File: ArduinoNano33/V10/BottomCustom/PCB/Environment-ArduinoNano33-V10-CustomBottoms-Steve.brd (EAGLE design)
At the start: 71 x 34 mm, 4 parts

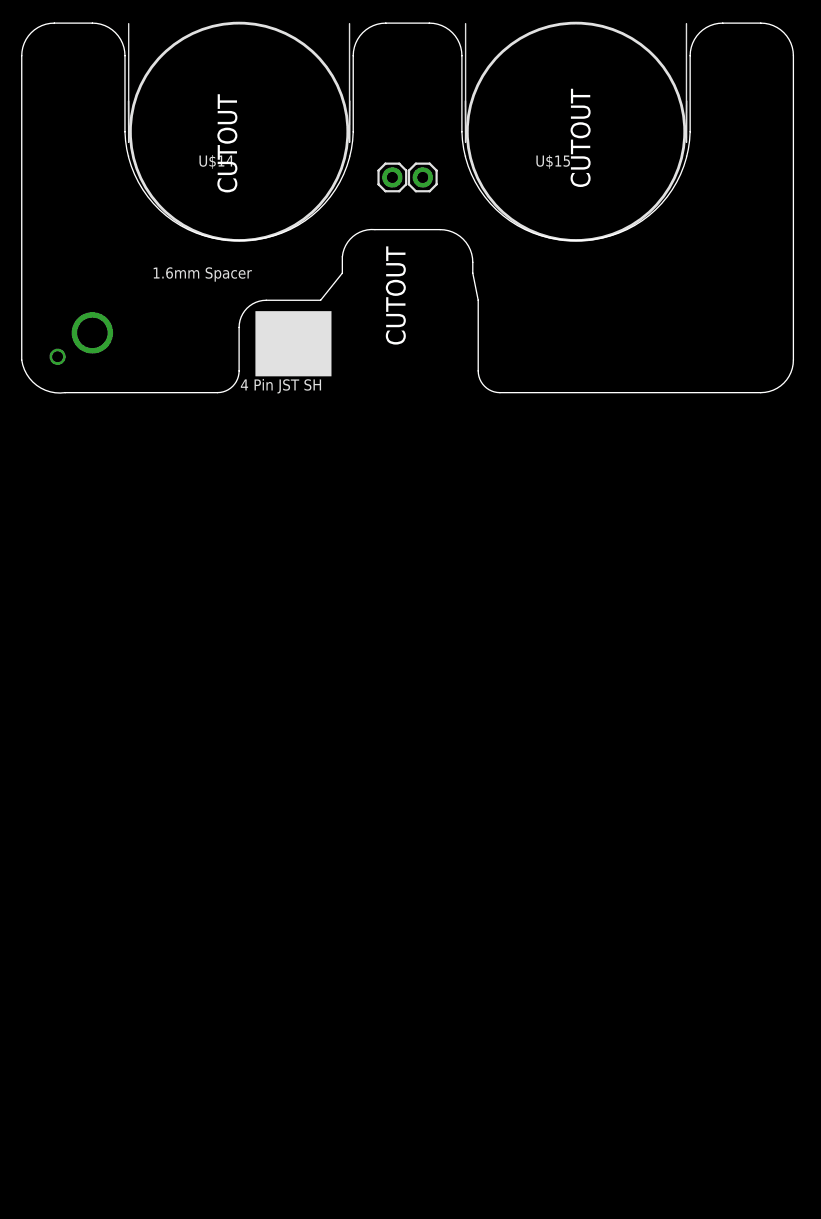
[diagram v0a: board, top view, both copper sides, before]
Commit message: Update for V10.1 with improvements...
* Removed USB C until I get a better foot print for the ones I can buy and replaced with Micro B
* Reduced cutout in middle layers as it doesn't need so much space.
* Increased hole size in middle layers for potential NFC wire passthrough to prevent clashes with solder
* Added potential extra solder connection for bottom to middle layers.
* Changed bottom boards so they use a top side pad to be soldered to rather than a hole to make the bottom face tidier.
* Removed switch on the top board as it would have been weird to use
* Added potential divider for the "3v3" supply to allow monitoring of battery voltage (although this may drain the battery too much)
* Extended the pads (where possible) for the Arduino to make hand soldering it to the board easier.
* Improved top level silk screen text
* Added "Up" to the bottom/middle layers to aid assembly.
* Fixed issue with missing holes on the non-key chain middle layer.
* Improved custom bottoms to be one PCB per customisation
* General tidy up of the reference lines
* Improved (fixed!) some of the filenames

Sent to JLCPCB - 27 Feb 2020
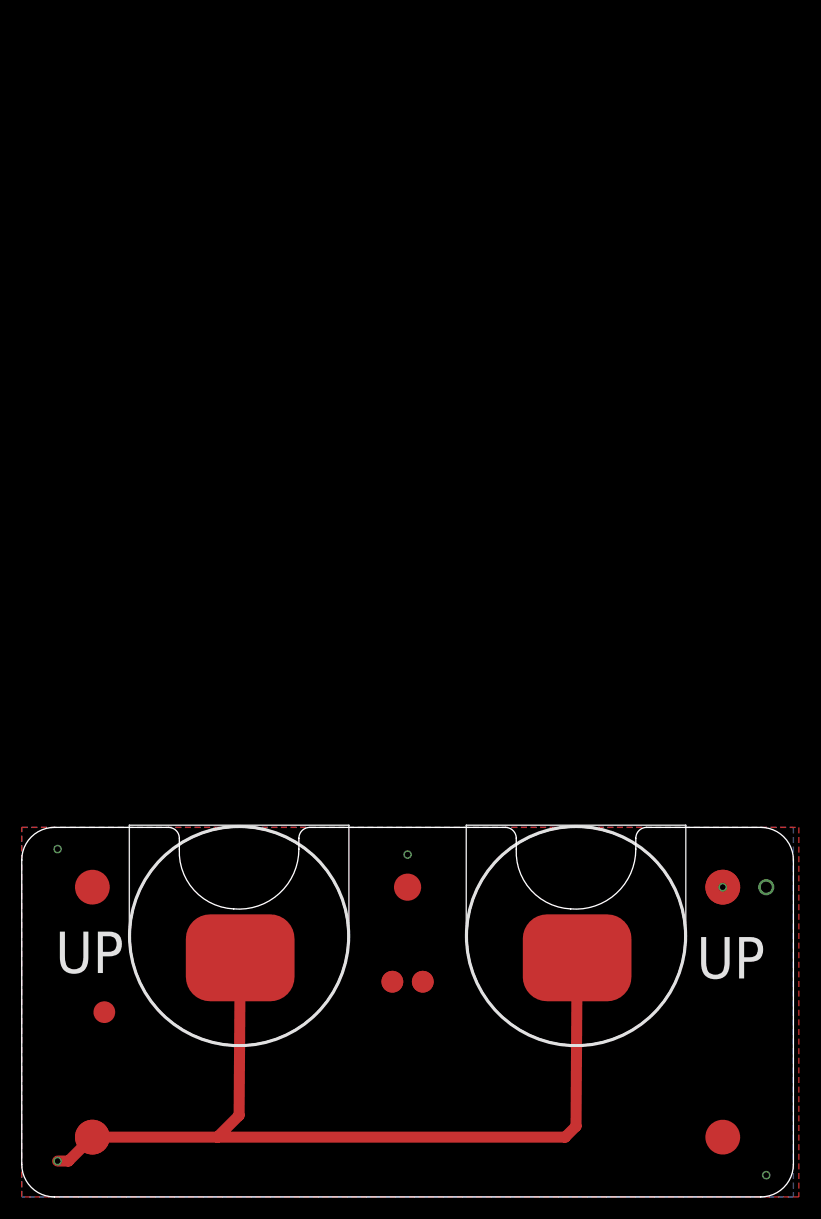
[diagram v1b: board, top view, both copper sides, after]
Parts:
- removed J7, J8: (no value), SparkFun-Connectors:1X01
- removed U$14, U$15: CR2032-SPLIT-PCB-MIDDLE, ThingySticks:CR2032-SMD-MIDDLE-OUTLINE
- added U$1: PERSONAL_ENVIRONMENT_SENSORTOP, ThingySticks:PERSONAL_ENVIRONMENT_SENSOR_TOP
- added U$11, U$7: CR2032-SPLIT-PCB-POSITIVE, ThingySticks:CR2032-SMD-POSITIVE-TERMINAL
- added U$2: PERSONAL_ENVIRONMENT_SENSORMIDDLE, ThingySticks:PERSONAL_ENVIRONMENT_SENSOR_MIDDLE_KEYRING
- added U$3: PERSONAL_ENVIRONMENT_SENSORBOTTOM, ThingySticks:PERSONAL_ENVIRONMENT_SENSOR_BOTTOM
- added U$4: PERSONAL_ENVIRONMENT_SENSORBOTTOM_TEMPLATE, ThingySticks:PERSONAL_ENVIRONMENT_SENSOR_BOTTOM_TEMPLATE
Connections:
- new net 3.3V: U$11.+, U$7.+
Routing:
- net 3.3V: track 0.00 -> 81.9 mm, vias 2 -> 1
- added copper zone on layer 1, net GND
- added copper zone on layer 16, net GND
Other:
- outline, holes or cut-outs redrawn
- board text added: "+"
- board text added: "Bottom PCB"
- board text added: "Steve"
- board text added: "ThingySticks"
- board text added: "ThingySticks Custom Name Base"
- board text added: "Top PCB has pads on solder side for battery -VE connection"
- board text removed: "1.6mm PCB"
- board text removed: "1.6mm Spacer"
- board text removed: "4 Pin JST SH"
- board text removed: "CUTOUT"
- board text removed: "Cable exit From under PCB to Front, then up to top"
- board text removed: "For Enclosure: Hammon - 1551V2WH - Plastic Enclosure, Small, ABS, 80 mm, 40 mm, 20 mm, IP30 Farnell: 2985869"
- board text removed: "Middle PCB"
